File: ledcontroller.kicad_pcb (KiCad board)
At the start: 2 copper layers, 60 x 38.8 mm, 42 parts, among them J1 Barrel_Jack, J2 RGBW analog, J3 RGB addressable, J4 Conn_01x05_Male, Q1 DMN3404L, Q2 DMN3404L, Q3 DMN3404L, Q4 DMN3404L, Q5 DMN3404L, Q6 DMN3404L, Q7 DMN3404L, Q8 DMN3404L, U1 TPS54233, U2 ESP32-WROOM-32

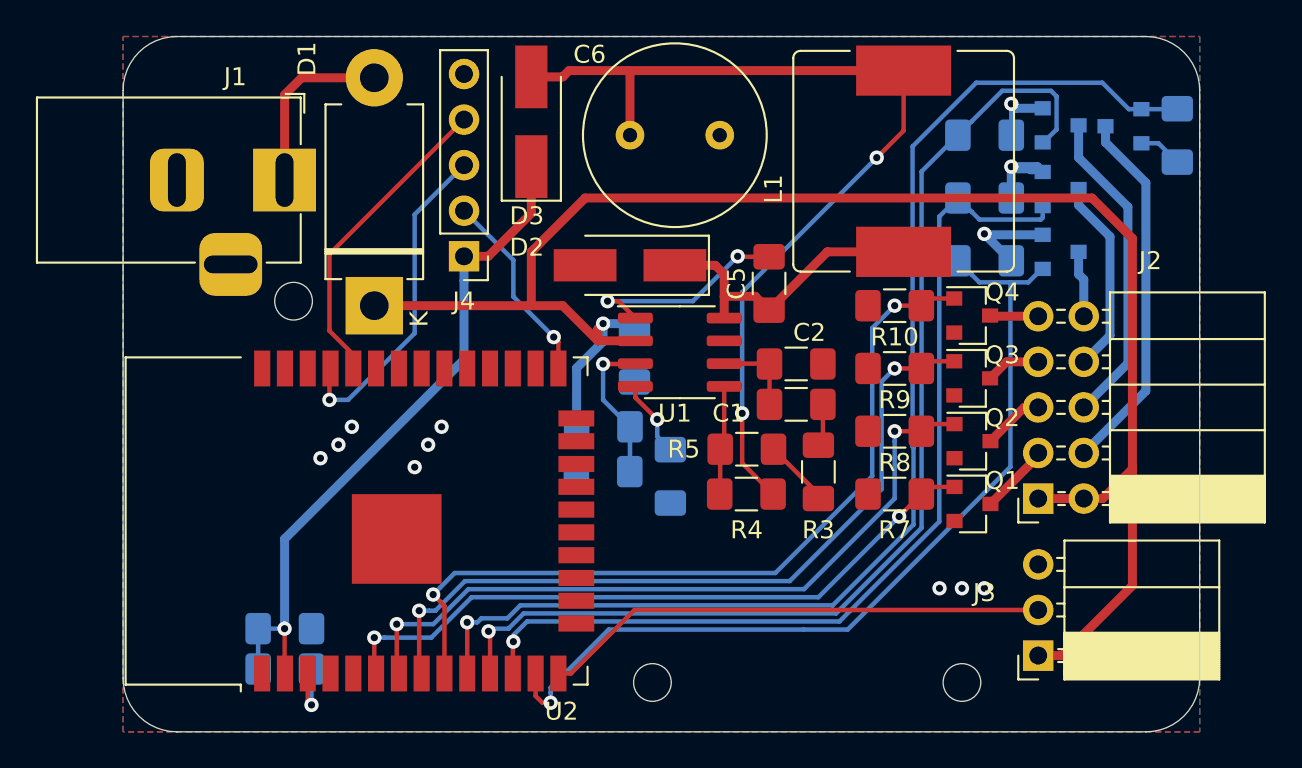
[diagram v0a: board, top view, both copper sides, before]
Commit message: Increase track width for power; release v1
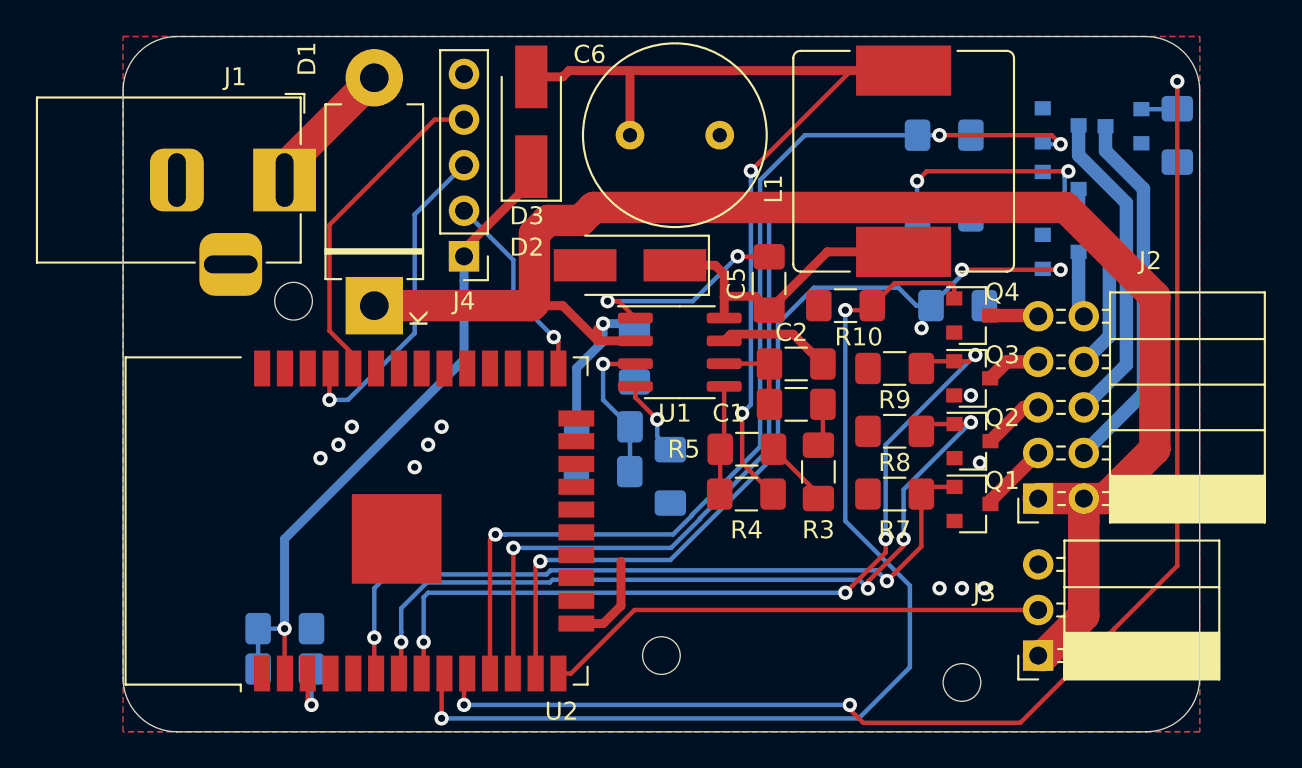
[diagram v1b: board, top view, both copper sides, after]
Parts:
- moved R14 2.92 mm to (146.5, 113.0)
- moved R10 2.74 mm to (140.3, 113.0)
- moved R13 2.46 mm to (145.8, 108.0)
- moved R12 2.25 mm to (145.8, 103.5)
- moved REF** 1.58 mm to (130.0, 132.5)
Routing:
- net /W1: track 45.6 -> 58.7 mm
- net /G2: track 67.9 -> 76.4 mm, vias 1 -> 3
- net /B2: track 52.9 -> 58.5 mm, vias 1 -> 3
- net GND: track 20.8 -> 15.6 mm
- net /B1: track 42.7 -> 47.7 mm, vias 2 -> 4
- net /R1: track 40.2 -> 44.8 mm, vias 2 -> 4
- net /G1: track 37.9 -> 41.7 mm
- net VPP: track 95.9 -> 92.1 mm
- net /R2: track 61.2 -> 58.4 mm, vias 1 -> 3
- net Net-(D1-Pad2): track 10.1 -> 7.77 mm
- net Net-(C6-Pad1): track 52.6 -> 54.3 mm
- net /W2: track 49.6 -> 48.4 mm, vias 1 -> 3
- net Net-(J4-Pad4): track 17.5 -> 18.5 mm
- net +3V3: track 38.5 -> 37.7 mm
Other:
- board text added: "https://github.com/mattsains/iot-led-strip v1.0"

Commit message: fixes #4 #3 #2
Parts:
- removed REF** (x3): MountingHole_2.1mm, MountingHole:MountingHole_2.1mm
- added  : MountingHole_2.2mm_M2, MountingHole:MountingHole_2.2mm_M2, F.Cu at (135.5, 127.0)
- added  : MountingHole_2.2mm_M2, MountingHole:MountingHole_2.2mm_M2, F.Cu at (123.0, 103.0)
- J4: value Conn_01x05_Male -> Conn_01x06_Male; footprint Connector_PinHeader_2.54mm:PinHeader_1x05_P2.54mm_Vertical -> Connector_PinHeader_2.54mm:PinHeader_1x06_P2.54mm_Vertical
- moved J4 33.1 mm to (143.0, 133.0), turned to 270 degrees
- moved D3 3.75 mm to (119.0, 102.8)
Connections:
- J4 pad 5: GND -> /EN
- R6 pad 2: Net-(R6-Pad2) -> /EN
- U2 pad 26: Net-(U2-Pad26) -> /W1
- U2 pad 27: Net-(U2-Pad27) -> /G1
- U2 pad 28: Net-(U2-Pad28) -> /B1
- U2 pad 3: Net-(R6-Pad2) -> /EN
- U2 pad 30: Net-(U2-Pad30) -> /R1
- U2 pad 6: /G1 -> Net-(U2-Pad6)
- U2 pad 7: /R1 -> Net-(U2-Pad7)
- U2 pad 8: /B1 -> Net-(U2-Pad8)
- U2 pad 9: /W1 -> Net-(U2-Pad9)
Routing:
- net +3V3: track 37.7 -> 76.5 mm, vias 1 -> 2
- net /EN: track 0.00 -> 27.8 mm, vias 0 -> 1
- net Net-(J4-Pad2): track 11.0 -> 36.6 mm
- net Net-(J4-Pad3): track 18.6 -> 40.0 mm
- net Net-(J4-Pad4): track 18.5 -> 35.6 mm, vias 0 -> 1
- net /R1: track 44.8 -> 56.7 mm
- net /G1: track 41.7 -> 51.4 mm
- net /B1: track 47.7 -> 51.8 mm, vias 4 -> 2
- net Net-(R6-Pad2): track 3.84 -> 0.00 mm, vias 1 -> 0
- net Net-(C6-Pad1): track 54.3 -> 58.0 mm
- net /W1: track 58.7 -> 57.2 mm
- net /R2: track 58.4 -> 57.5 mm
- net /B2: track 58.5 -> 57.7 mm
- net VPP: track 92.1 -> 92.7 mm
- net /G2: track 76.4 -> 76.7 mm, vias 3 -> 1
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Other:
- board text added: "https://github.com/mattsains/iot-led-strip v1.1"
- board text removed: "https://github.com/mattsains/iot-led-strip v1.0"

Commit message: respin for v1.1
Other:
- board text added: "3.3V"
- board text added: "EN"
- board text added: "GND"
- board text added: "GP0"
- board text added: "RX"
- board text added: "TX"
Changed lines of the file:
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@@
   (general
     (thickness 1.6)
-    (drawings 9)
+    (drawings 15)
     (tracks 338)
     (zones 0)
@@
   (page A4)
   (layers
-    (0 F.Cu signal hide)
-    (31 B.Cu signal hide)
-    (32 B.Adhes user hide)
-    (33 F.Adhes user hide)
-    (34 B.Paste user hide)
-    (35 F.Paste user hide)
+    (0 F.Cu signal)
+    (31 B.Cu signal)
+    (32 B.Adhes user)
+    (33 F.Adhes user)
+    (34 B.Paste user)
+    (35 F.Paste user)
     (36 B.SilkS user)
-    (37 F.SilkS user hide)
-    (38 B.Mask user hide)
-    (39 F.Mask user hide)
-    (40 Dwgs.User user hide)
-    (41 Cmts.User user hide)
-    (42 Eco1.User user hide)
-    (43 Eco2.User user hide)
-    (44 Edge.Cuts user hide)
-    (45 Margin user hide)
-    (46 B.CrtYd user hide)
-    (47 F.CrtYd user hide)
-    (48 B.Fab user hide)
-    (49 F.Fab user hide)
+    (37 F.SilkS user)
+    (38 B.Mask user)
+    (39 F.Mask user)
+    (40 Dwgs.User user)
+    (41 Cmts.User user)
+    (42 Eco1.User user)
+    (43 Eco2.User user)
+    (44 Edge.Cuts user)
+    (45 Margin user)
+    (46 B.CrtYd user)
+    (47 F.CrtYd user)
+    (48 B.Fab user)
+    (49 F.Fab user)
   )
   (setup
@@
     )
   )
-  (gr_text "https://github.com/mattsains/iot-led-strip\nv1.1" (at 129 128) (layer B.SilkS)
+  (gr_text 3.3V (at 143 135.5) (layer F.SilkS)
+    (effects (font (size 0.7 0.7) (thickness 0.15)))
+  )
+  (gr_text GP0 (at 140.5 135.5) (layer F.SilkS)
+    (effects (font (size 0.7 0.7) (thickness 0.15)))
+  )
+  (gr_text TX (at 138 135.5) (layer F.SilkS)
+    (effects (font (size 0.7 0.7) (thickness 0.15)))
+  )
+  (gr_text RX (at 135.25 135.5) (layer F.SilkS)
+    (effects (font (size 0.7 0.7) (thickness 0.15)))
+  )
+  (gr_text EN (at 132.75 135.5) (layer F.SilkS)
+    (effects (font (size 0.7 0.7) (thickness 0.15)))
+  )
+  (gr_text GND (at 130.25 135.5) (layer F.SilkS)
+    (effects (font (size 0.7 0.7) (thickness 0.15)))
+  )
+  (gr_text "https://github.com/mattsains/iot-led-strip\nv1.1" (at 129 130.5) (layer B.SilkS)
     (effects (font (size 1 1) (thickness 0.15)) (justify mirror))
   )
@@
   (segment (start 151 129.96) (end 128.5 129.96) (width 0.25) (layer F.Cu) (net 15))
   (segment (start 128.5 129.96) (end 124.96 133.5) (width 0.25) (layer F.Cu) (net 15))
-  (via (at 110.5 135.25) (size 0.8) (drill 0.4) (layers F.Cu B.Cu) (net 50))
-  (segment (start 110.29 133.5) (end 110.29 135.04) (width 0.25) (layer F.Cu) (net 50))
-  (segment (start 110.29 135.04) (end 110.5 135.25) (width 0.25) (layer F.Cu) (net 50))
-  (segment (start 110.5 135.25) (end 110.5 133.25) (width 0.25) (layer B.Cu) (net 50))
   (segment (start 144.8875 123.1) (end 144.4875 123.5) (width 0.25) (layer F.Cu) (net 33))
   (segment (start 146.336 123.1) (end 144.8875 123.1) (width 0.25) (layer F.Cu) (net 33))
@@
   (segment (start 144 128) (end 144 125.565685) (width 0.25) (layer B.Cu) (net 33))
   (segment (start 120.51266 113.51266) (end 119 115.02532) (width 0.25) (layer B.Cu) (net 33))
-  (segment (start 114 133.4) (end 114.1 133.5) (width 0.25) (layer F.Cu) (net 54))
-  (segment (start 115.25 133.38) (end 115.37 133.5) (width 0.25) (layer F.Cu) (net 53))
   (segment (start 146.336 119.6) (end 146.286 119.6) (width 0.25) (layer F.Cu) (net 34))
   (segment (start 146.336 119.6) (end 144.8875 119.6) (width 0.25) (layer F.Cu) (net 34))
-  (segment (start 115.5 133.37) (end 115.37 133.5) (width 0.25) (layer F.Cu) (net 53))
   (via (at 147.25 119.5) (size 0.8) (drill 0.4) (layers F.Cu B.Cu) (net 34))
   (segment (start 146.336 119.6) (end 147.15 119.6) (width 0.25) (layer F.Cu) (net 34))
@@
   (segment (start 122 113.5) (end 120.999998 114.500002) (width 0.25) (layer B.Cu) (net 34))
   (segment (start 120.999998 126.636409) (end 123.813599 129.450009) (width 0.25) (layer B.Cu) (net 34))
-  (segment (start 116.5 133.36) (end 116.64 133.5) (width 0.25) (layer F.Cu) (net 52))
   (segment (start 144.8875 116.1) (end 144.4875 116.5) (width 0.25) (layer F.Cu) (net 35))
   (segment (start 146.32 116.1) (end 144.8875 116.1) (width 0.25) (layer F.Cu) (net 35))
   (segment (start 144.4875 116.5) (end 144.4875 116.5125) (width 0.25) (layer F.Cu) (net 35))
-  (segment (start 116.75 133.39) (end 116.64 133.5) (width 0.25) (layer F.Cu) (net 52))
   (via (at 147.5 115.75) (size 0.8) (drill 0.4) (layers F.Cu B.Cu) (net 35))
   (segment (start 146.32 116.1) (end 147.15 116.1) (width 0.25) (layer F.Cu) (net 35))
@@
   (segment (start 142.099978 121.150022) (end 147.100001 116.149999) (width 0.25) (layer B.Cu) (net 35))
   (segment (start 147.100001 116.149999) (end 147.5 115.75) (width 0.25) (layer B.Cu) (net 35))
-  (segment (start 117.75 133.66) (end 117.91 133.5) (width 0.25) (layer F.Cu) (net 51))
   (segment (start 146.32 111.95) (end 146.12 111.75) (width 0.25) (layer F.Cu) (net 36))
   (segment (start 146.32 112.6) (end 146.32 111.95) (width 0.25) (layer F.Cu) (net 36))
@@
   (segment (start 139.610001 132.150001) (end 140.46 133) (width 0.25) (layer B.Cu) (net 49))
   (segment (start 119 127) (end 122.90002 130.90002) (width 0.25) (layer B.Cu) (net 49))
+  (via (at 110.5 135.25) (size 0.8) (drill 0.4) (layers F.Cu B.Cu) (net 50))
+  (segment (start 110.29 133.5) (end 110.29 135.04) (width 0.25) (layer F.Cu) (net 50))
+  (segment (start 110.29 135.04) (end 110.5 135.25) (width 0.25) (layer F.Cu) (net 50))
+  (segment (start 110.5 135.25) (end 110.5 133.25) (width 0.25) (layer B.Cu) (net 50))
   (segment (start 110.5 135.25) (end 131.75 135.25) (width 0.25) (layer B.Cu) (net 50))
   (segment (start 131.75 135.25) (end 132 135) (width 0.25) (layer B.Cu) (net 50))
@@
   (segment (start 131.990001 134.990001) (end 131.990001 133.849999) (width 0.25) (layer B.Cu) (net 50))
   (segment (start 132 135) (end 131.990001 134.990001) (width 0.25) (layer B.Cu) (net 50))
+  (segment (start 117.75 133.66) (end 117.91 133.5) (width 0.25) (layer F.Cu) (net 51))
+  (segment (start 116.5 133.36) (end 116.64 133.5) (width 0.25) (layer F.Cu) (net 52))
+  (segment (start 116.75 133.39) (end 116.64 133.5) (width 0.25) (layer F.Cu) (net 52))
+  (segment (start 115.25 133.38) (end 115.37 133.5) (width 0.25) (layer F.Cu) (net 53))
+  (segment (start 115.5 133.37) (end 115.37 133.5) (width 0.25) (layer F.Cu) (net 53))
+  (segment (start 114 133.4) (end 114.1 133.5) (width 0.25) (layer F.Cu) (net 54))
   (zone (net 3) (net_name GND) (layer F.Cu) (hatch edge 0.508)
     (connect_pads (clearance 0.508))
